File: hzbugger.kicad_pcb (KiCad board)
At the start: 2 copper layers, 55.4 x 26.7 mm, 51 parts, among them J2 IDC, J4 SWD, J6 GPIO, SW1 RESET_SW, U1 STM32F103C8T6, U2 SRV05-4, U3 AMS1117-3.3, U4 HX AM 90D, Y1 8M

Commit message: routing
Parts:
- added SW2: BOOT0_SW, hzbugger:SW-SMD_4P-L5.1-W5.1-P3.70-LS6.5-TL_H1.5, F.Cu at (135.5, 96.8)
- J6: footprint hzbugger:SMD-PinHeader_1x06_P2.54mm_Vertical -> Connector_PinHeader_2.54mm:PinHeader_1x06_P2.54mm_Vertical
- moved C14 10.4 mm to (150.2, 79.0), turned to 0 degrees
- moved R1 10.0 mm to (119.8, 94.0), turned to 180 degrees
- moved J6 7.94 mm to (116.2, 96.5)
- moved C2 2.31 mm to (112.5, 94.5)
- moved R8 1.07 mm to (134.2, 93.0)
- moved R2 0.56 mm to (131.5, 93.5)
- moved R14 0.55 mm to (132.5, 93.5)
- moved C16 0.41 mm to (137.8, 93.0), turned to 0 degrees
- moved SW1 0.37 mm to (144.1, 95.8)
- moved C10 0.21 mm to (127.1, 90.8)
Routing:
- net +5V: track 8.48 -> 48.3 mm, vias 0 -> 2
- net SWDIO: track 12.0 -> 33.4 mm
- net SPI1_SCK: track 3.15 -> 13.0 mm
- net Net-(J6-Pin_3): track 3.50 -> 11.7 mm
- net +3V3: track 130.7 -> 135.2 mm, vias 8 -> 7
- net GND: track 118.3 -> 113.9 mm, vias 126 -> 123
- net Net-(J6-Pin_4): track 2.56 -> 0.00 mm
- net unconnected-(U1-PB9-Pad46): track 2.41 -> 0.00 mm
- net DCLK: track 16.1 -> 14.0 mm, vias 2 -> 0
- net RST: track 21.1 -> 23.1 mm, vias 0 -> 1
- net Net-(J6-Pin_2): track 4.44 -> 2.72 mm
- net Net-(U1-BOOT0): track 2.58 -> 1.66 mm
- net SPI1_MISO: track 2.80 -> 2.27 mm
- net SPI1_MOSI: track 2.59 -> 2.06 mm
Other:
- board text added: "8M"
- board text added: "B"
- board text added: "pin1"
- board text removed: "pin 1"

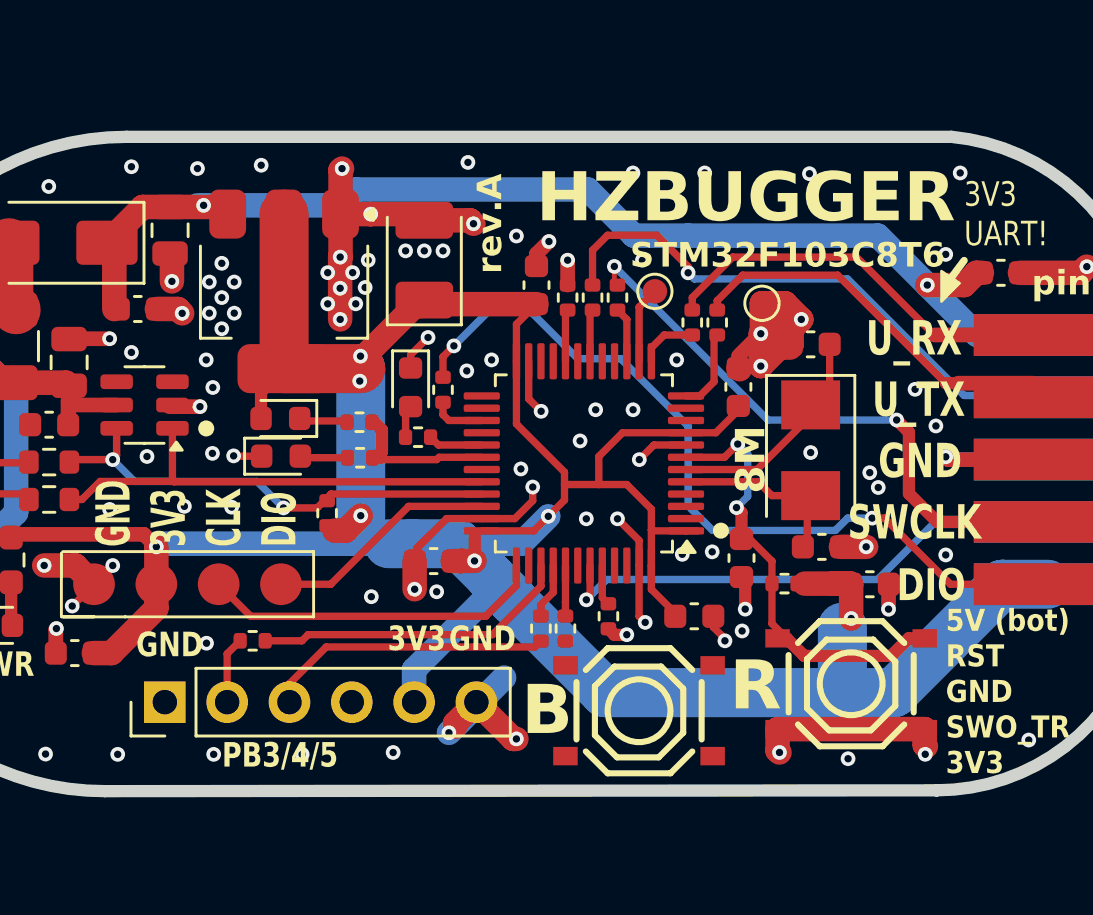
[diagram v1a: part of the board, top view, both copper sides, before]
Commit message: usr led
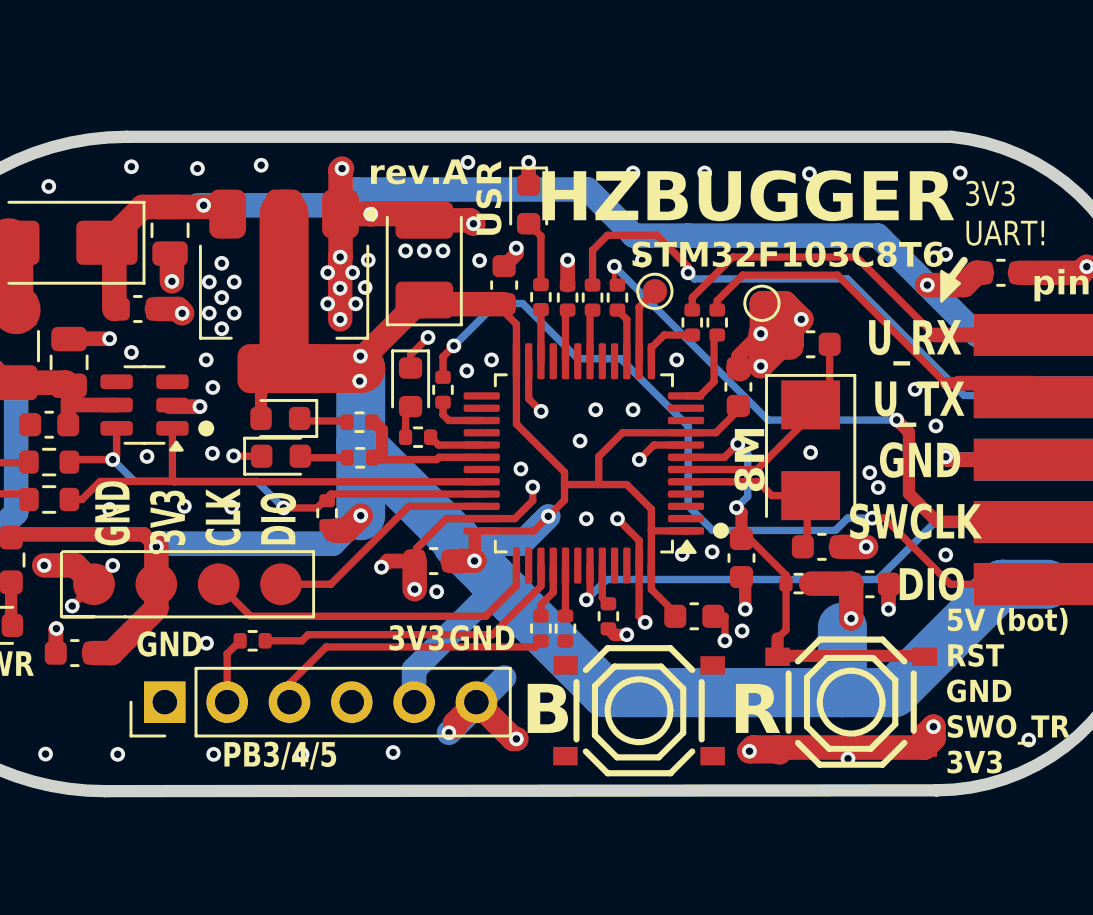
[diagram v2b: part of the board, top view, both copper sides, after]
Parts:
- added D6: LED1, LED_SMD:LED_0603_1608Metric, F.Cu at (131.0, 76.2)
- added R19: 1k5, Resistor_SMD:R_0402_1005Metric, F.Cu at (131.5, 80.0)
- moved C7 1.32 mm to (130.0, 79.5)
- moved SW1 0.75 mm to (144.1, 96.5)
- moved R7 0.57 mm to (142.0, 91.7)
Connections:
- U1 pad 22: unconnected-(U1-PB11-Pad22) -> Net-(U1-PB11)
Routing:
- net GND: track 113.9 -> 119.0 mm, vias 123 -> 124
- net +3V3: track 135.2 -> 139.0 mm
- net Net-(D6-A): track 0.00 -> 2.69 mm
- net Net-(U1-PB11): track 0.00 -> 2.11 mm
- net Net-(SW1-A): track 18.0 -> 19.4 mm
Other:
- board text added: "USR"

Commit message: DRC
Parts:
- moved R1 10.3 mm to (130.0, 93.0), turned to -135 degrees
- moved R2 0.35 mm to (131.2, 93.2), turned to -135 degrees
- moved R8 0.25 mm to (134.5, 93.0), turned to 0 degrees
- moved R18 0.05 mm to (126.5, 85.8)
- turned R14 to -135 degrees
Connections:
- R8 pad 1: Net-(U1-BOOT0) -> Net-(SW2-A)
- SW2 pad 1: unconnected-(SW2-A-Pad1) -> Net-(SW2-A)
- SW2 pad 2: unconnected-(SW2-B-Pad2) -> Net-(SW2-A)
- SW2 pad 3: unconnected-(SW2-C-Pad3) -> +3V3
- U1 pad 44: Net-(U1-BOOT0) -> Net-(SW2-A)
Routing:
- net Net-(SW2-A): track 0.00 -> 12.1 mm
- net SPI1_SCK: track 13.0 -> 2.34 mm
- net GND: track 119.0 -> 129.5 mm, vias 124 -> 143
- net Net-(J6-Pin_2): track 2.72 -> 12.2 mm
- net Net-(J6-Pin_4): track 0.00 -> 9.44 mm
- net +3V3: track 139.0 -> 142.9 mm, vias 7 -> 8
- net Net-(U1-BOOT0): track 1.66 -> 0.00 mm
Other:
- board text added: "5V (bot) RST GND SWO_T 3V3"
- board text added: "PB 3/4/5"
- board text added: "rev.A 2026"
- board text removed: "5V (bot) RST GND SWO_TR 3V3"
- board text removed: "rev.A"

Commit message: routing
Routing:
- net GND: vias 143 -> 145
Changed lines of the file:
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@@
 	(footprint "Resistor_SMD:R_0402_1005Metric"
 		(layer "F.Cu")
-		(at 124.1298 86.5378 180)
+		(at 124.1298 86.5 180)
 		(descr "Resistor SMD 0402 (1005 Metric), square (rectangular) end terminal, IPC_7351 nominal, (Body size source: IPC-SM-782 page 72, https://www.pcb-3d.com/wordpress/wp-content/uploads/ipc-sm-782a_amendment_1_and_2.pdf), generated with kicad-footprint-generator")
 		(tags "resistor")
@@
 	)
 	(gr_text "R"
-		(at 140.25 98 0)
+		(at 140 97.75 0)
 		(layer "F.SilkS")
 		(effects
@@
 	)
 	(gr_text "B"
-		(at 131.75 98 0)
+		(at 131.5 98 0)
 		(layer "F.SilkS")
 		(effects
@@
 	)
 	(via
+		(at 130.25 96)
+		(size 0.6)
+		(drill 0.3)
+		(layers "F.Cu" "B.Cu")
+		(net 9)
+	)
+	(via
 		(at 131.1656 87.7316)
 		(size 0.6)
@@
 	)
 	(via
+		(at 131.5 96.25)
+		(size 0.6)
+		(drill 0.3)
+		(layers "F.Cu" "B.Cu")
+		(free yes)
+		(net 9)
+	)
+	(via
 		(at 127.508 78.105)
 		(size 0.6)
@@
 	(segment
 		(start 128 97.5)
-		(end 130 95.5)
+		(end 129.5 96)
 		(width 1)
 		(layer "B.Cu")
@@
 	)
 	(segment
+		(start 129.5 96)
+		(end 130.25 96)
+		(width 1)
+		(layer "B.Cu")
+		(net 9)
+	)
+	(segment
 		(start 136 79.9)
 		(end 136.144 79.756)
@@
 	)
 	(segment
-		(start 124.6398 86.5378)
-		(end 124.9548 86.5378)
+		(start 127.434 86.75)
+		(end 127.665 86.519)
 		(width 0.3)
 		(layer "F.Cu")
@@
 	)
 	(segment
-		(start 127.349 86.519)
+		(start 127.665 86.519)
 		(end 129.089 86.519)
 		(width 0.3)
@@
 	)
 	(segment
-		(start 127.118 86.75)
-		(end 127.349 86.519)
-		(width 0.3)
-		(layer "F.Cu")
-		(net 45)
-	)
-	(segment
 		(start 125.167 86.75)
-		(end 127.118 86.75)
+		(end 127.434 86.75)
 		(width 0.3)
 		(layer "F.Cu")
@@
 	)
 	(segment
-		(start 121.756595 86.5378)
-		(end 121.693544 86.474749)
+		(start 124.6398 86.5)
+		(end 124.6776 86.5378)
+		(width 0.3)
+		(layer "F.Cu")
+		(net 45)
+	)
+	(segment
+		(start 124.6776 86.5378)
+		(end 124.9548 86.5378)
+		(width 0.3)
+		(layer "F.Cu")
+		(net 45)
+	)
+	(segment
+		(start 123.6198 86.5)
+		(end 123.582 86.5378)
 		(width 0.3)
 		(layer "F.Cu")
@@
 	)
 	(segment
-		(start 123.6198 86.5378)
+		(start 123.582 86.5378)
 		(end 121.756595 86.5378)
 		(width 0.3)
 		(layer "F.Cu")
+		(net 46)
+	)
+	(segment
+		(start 121.756595 86.5378)
+		(end 121.693544 86.474749)
+		(width 0.3)
+		(layer "F.Cu")

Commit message: silks etc
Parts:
- moved SW2 0.15 mm to (135.5, 97.0)
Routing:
- net GND: track 129.5 -> 128.7 mm, vias 145 -> 148
- net +5V: track 48.3 -> 47.7 mm
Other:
- board text added: "+5V (bot) RST GND SWO_T 3V3"
- board text added: "A4"
- board text added: "G"
- board text removed: "5V (bot) RST GND SWO_T 3V3"

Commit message: minor
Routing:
- net GND: vias 148 -> 149
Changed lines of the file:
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@@
 	(footprint "LED_SMD:LED_0603_1608Metric"
 		(layer "F.Cu")
-		(at 120.906044 86.474749)
+		(at 120.906044 86.5)
 		(descr "LED SMD 0603 (1608 Metric), square (rectangular) end terminal, IPC_7351 nominal, (Body size source: http://www.tortai-tech.com/upload/download/2011102023233369053.pdf), generated with kicad-footprint-generator")
 		(tags "LED")
@@
 	)
 	(segment
+		(start 118.986749 86.474749)
+		(end 118.9736 86.4616)
+		(width 0.3)
+		(layer "F.Cu")
+		(net 9)
+	)
+	(segment
 		(start 140.462 82.804)
 		(end 140.462 81.4832)
@@
 	)
 	(segment
+		(start 120.118544 86.5)
+		(end 120.093293 86.474749)
+		(width 0.3)
+		(layer "F.Cu")
+		(net 9)
+	)
+	(segment
 		(start 105.06 93.249)
 		(end 105.045 93.249)
@@
 	)
 	(segment
-		(start 118.986749 86.474749)
-		(end 118.9736 86.4616)
-		(width 0.3)
-		(layer "F.Cu")
-		(net 9)
-	)
-	(segment
 		(start 134.62 89.027)
 		(end 135.5015 89.9085)
@@
 	)
 	(segment
+		(start 120.093293 86.474749)
+		(end 118.986749 86.474749)
+		(width 0.3)
+		(layer "F.Cu")
+		(net 9)
+	)
+	(segment
 		(start 126.352 91.5)
 		(end 126.352 90.75)
@@
 		(net 9)
 	)
-	(segment
-		(start 120.118544 86.474749)
-		(end 118.986749 86.474749)
-		(width 0.3)
-		(layer "F.Cu")
-		(net 9)
-	)
 	(via
 		(at 147.5994 85.2424)
@@
 	)
 	(via
+		(at 105.5 83.5)
+		(size 0.6)
+		(drill 0.3)
+		(layers "F.Cu" "B.Cu")
+		(free yes)
+		(net 9)
+	)
+	(via
 		(at 123.317 80.899)
 		(size 0.6)
@@
 	)
 	(segment
-		(start 152.146 81.534)
-		(end 149.284 81.534)
+		(start 137.25 76.25)
+		(end 117.75 76.25)
 		(width 1)
 		(layer "B.Cu")
@@
 	)
 	(segment
-		(start 149.284 81.534)
-		(end 147.25 79.5)
+		(start 152.146 81.534)
+		(end 149.284 81.534)
 		(width 1)
 		(layer "B.Cu")
@@
 	)
 	(segment
-		(start 134.053628 76.25)
-		(end 117.75 76.25)
+		(start 149.284 81.534)
+		(end 147.25 79.5)
 		(width 1)
 		(layer "B.Cu")
@@
 	)
 	(segment
-		(start 135.288628 77.485)
-		(end 134.053628 76.25)
+		(start 138.485 77.485)
+		(end 137.25 76.25)
 		(width 1)
 		(layer "B.Cu")
@@
 	(segment
 		(start 145.235 77.485)
-		(end 135.288628 77.485)
+		(end 138.485 77.485)
 		(width 1)
 		(layer "B.Cu")
@@
 	)
 	(segment
-		(start 123.6198 86.5)
-		(end 123.582 86.5378)
+		(start 121.756595 86.5378)
+		(end 121.718795 86.5)
+		(width 0.3)
+		(layer "F.Cu")
+		(net 46)
+	)
+	(segment
+		(start 121.718795 86.5)
+		(end 121.693544 86.5)
 		(width 0.3)
 		(layer "F.Cu")
@@
 	)
 	(segment
-		(start 121.756595 86.5378)
-		(end 121.693544 86.474749)
+		(start 123.6198 86.5)
+		(end 123.582 86.5378)
 		(width 0.3)
 		(layer "F.Cu")

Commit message: some fine-tuning
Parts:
- moved C14 0.72 mm to (150.2, 78.3), turned to 90 degrees
- moved C11 0.26 mm to (142.2, 82.0)
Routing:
- net GND: track 128.7 -> 127.3 mm, vias 149 -> 148
- net +5V: track 47.7 -> 48.5 mm
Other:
- board text added: "3V3!"
- board text added: "F103 C8T6"
- board text added: "rev.A '26"
- board text removed: "3V3 UART!"
- board text removed: "STM32F103C8T6"
- board text removed: "rev.A 2026"

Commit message: layout enhancements
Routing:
- net GND: track 127.3 -> 140.0 mm, vias 148 -> 156
